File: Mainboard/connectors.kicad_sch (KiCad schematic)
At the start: 19 parts, among them J601 ADIRS backlight, J602 FUEL backlight, J603 ELEC backlight, J604 GPWS backlight, J605 AIRCOND backlight, J606 EXTLT backlight, J607 APU backlight, J608 SIGNS backlight, J701 ADIRS ribbon, J702 FUEL ribbon, J703 ELEC ribbon, J704 GPWS ribbon, J705 AIRCOND ribbon, J706 EXTLT ribbon, J707 APU ribbon, J708 SIGNS ribbon, Q601 IRLIZ44N

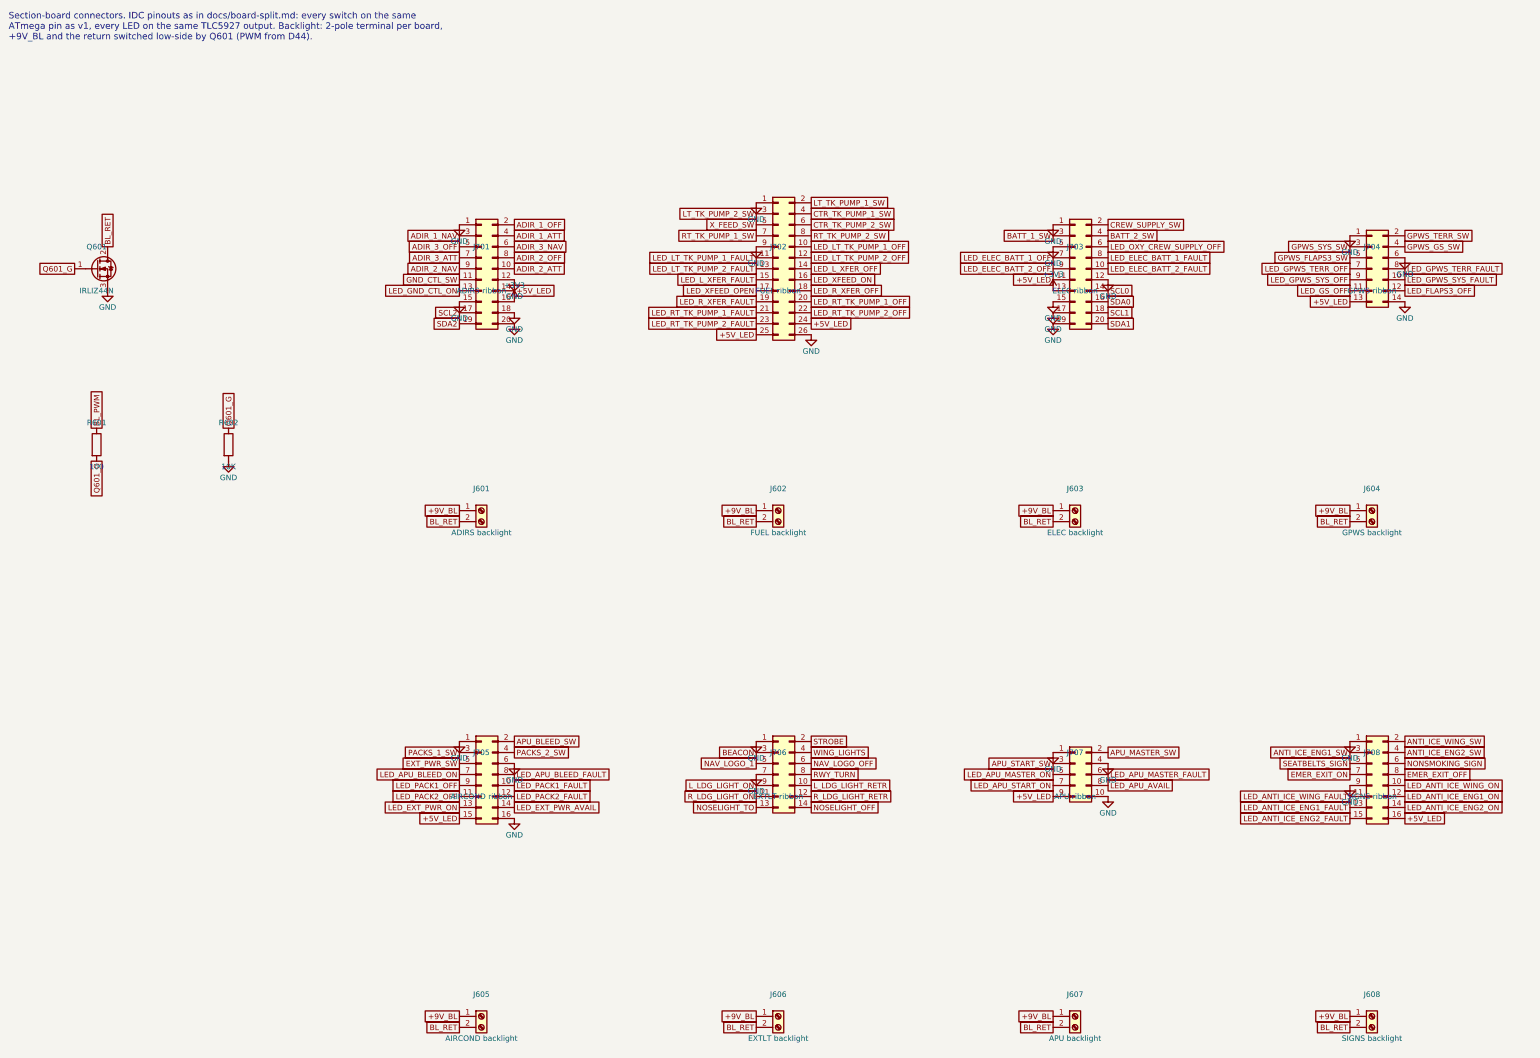
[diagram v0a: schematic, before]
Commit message: Lay the mainboard schematic out so that nothing overlaps
Reference and value now sit outside each symbol (above and below, or beside
it for parts whose pins leave up and down), turned horizontal on rotated
parts. GND on a sideways pin is a label instead of a power symbol that
crowded the neighbouring pins. The annunciator sheet keeps its four TLC5927
in two wider columns, their R-EXT and capacitors in a row underneath, the
series resistors horizontal on the right and both supply switches along the
bottom, all inside the frame. The connector sheet has wider columns.

Layout only: the netlist is identical to the previous commit (126 parts,
230 nets, same values, footprints and fields), and ERC is still clean.

Co-Authored-By: Claude Opus 5.5 <noreply@anthropic.com>
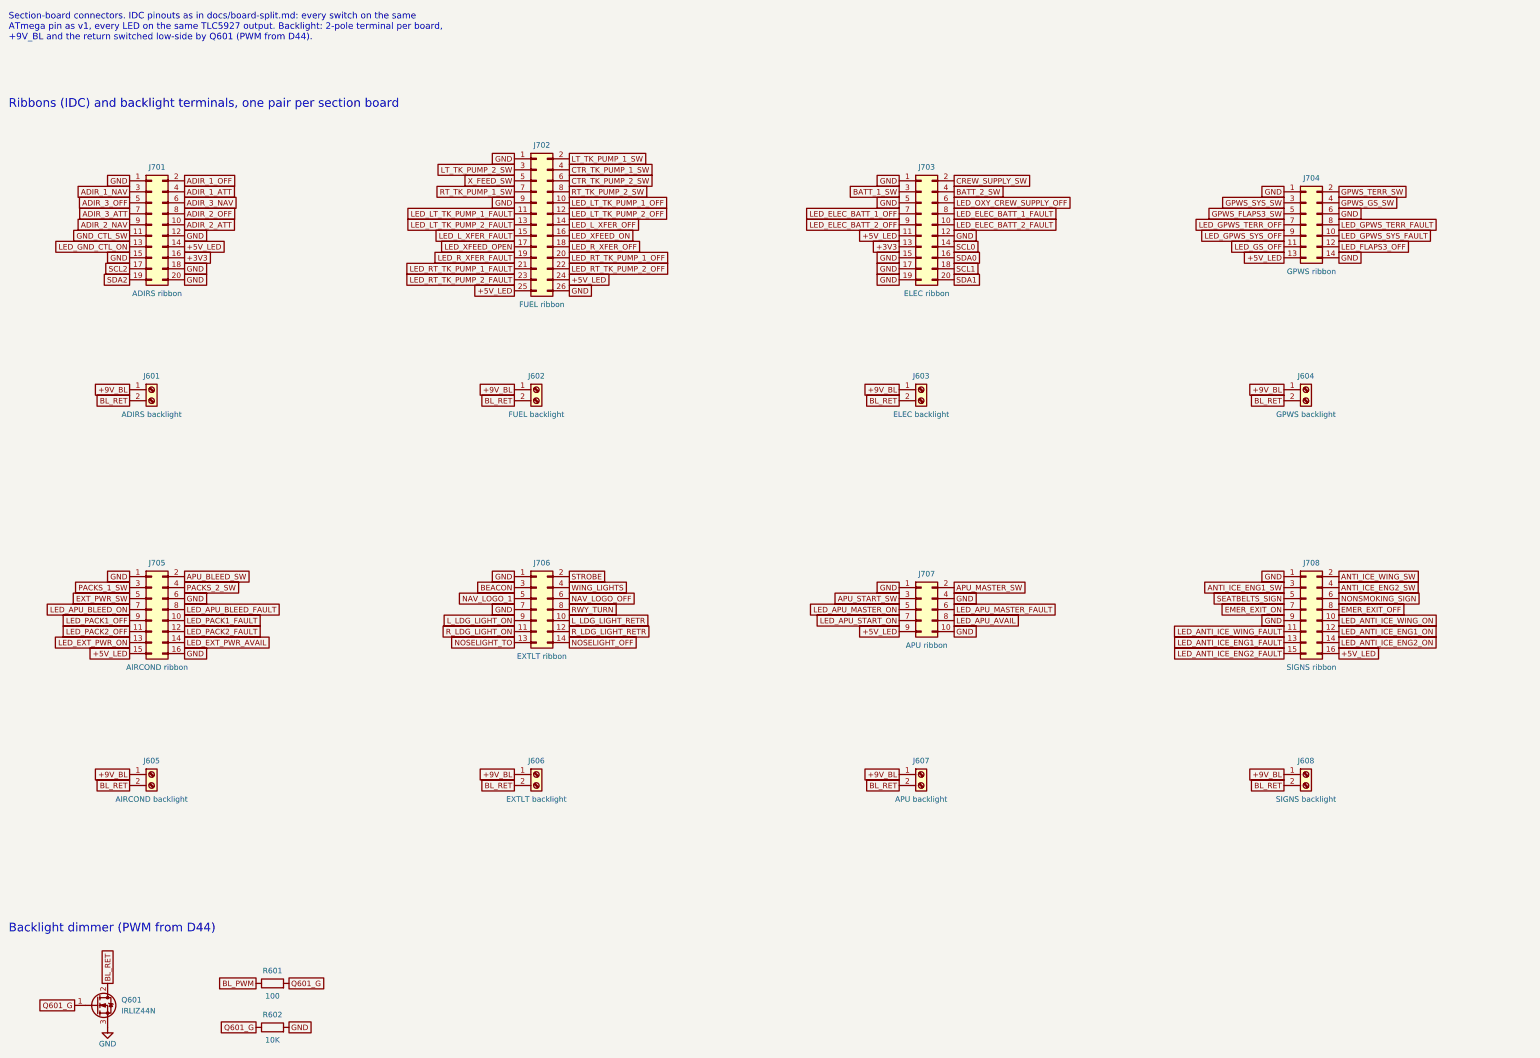
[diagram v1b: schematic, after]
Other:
- note added: "Backlight dimmer (PWM from D44)"
- note added: "Ribbons (IDC) and backlight terminals, one pair per section board"

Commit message: Mainboard schematic: 3.5 mm backlight terminals, IRLIZ44N lying flat
The eight backlight terminals become Phoenix PT 1,5/2-3,5 (22-24 AWG, 1.1 A
in all), so they fit along one edge of the 137 x 89 mm mainboard; the 9 V
input keeps its 5.08 mm terminal. The IRLIZ44N lies flat (TO-220F
horizontal): 1.1 A needs no heatsink, and it stays well below the section
boards. F101's note now says ~1.1 A (63 strings at 17 mA). The netlist
changes only in those nine footprints. The TLC5927 footprint drops a
duplicated pin-1 asterisk. Net classes set for the mainboard layout.

EXT LT: J2 moves next to J1, over the low part of the mainboard.

Co-Authored-By: Claude Opus 5.5 <noreply@anthropic.com>
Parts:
- J601, J602, J603, J604, J605, J606, J607, J608: footprint TerminalBlock_Phoenix:TerminalBlock_Phoenix_MKDS-1,5-2-5.08_1x02_P5.08mm_Horizontal -> TerminalBlock_Phoenix:TerminalBlock_Phoenix_PT-1,5-2-3.5-H_1x02_P3.50mm_Horizontal
- Q601: footprint Package_TO_SOT_THT:TO-220F-3_Vertical -> Package_TO_SOT_THT:TO-220F-3_Horizontal_TabDown
